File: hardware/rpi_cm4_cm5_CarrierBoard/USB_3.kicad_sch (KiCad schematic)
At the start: 74 parts, among them J2 0484050003, J3 0484050003, U6 SST25VF512A, U7 UPD720202K8-711-BAA-A, U8 AP2192AFGEG-7, Y1 24MHz

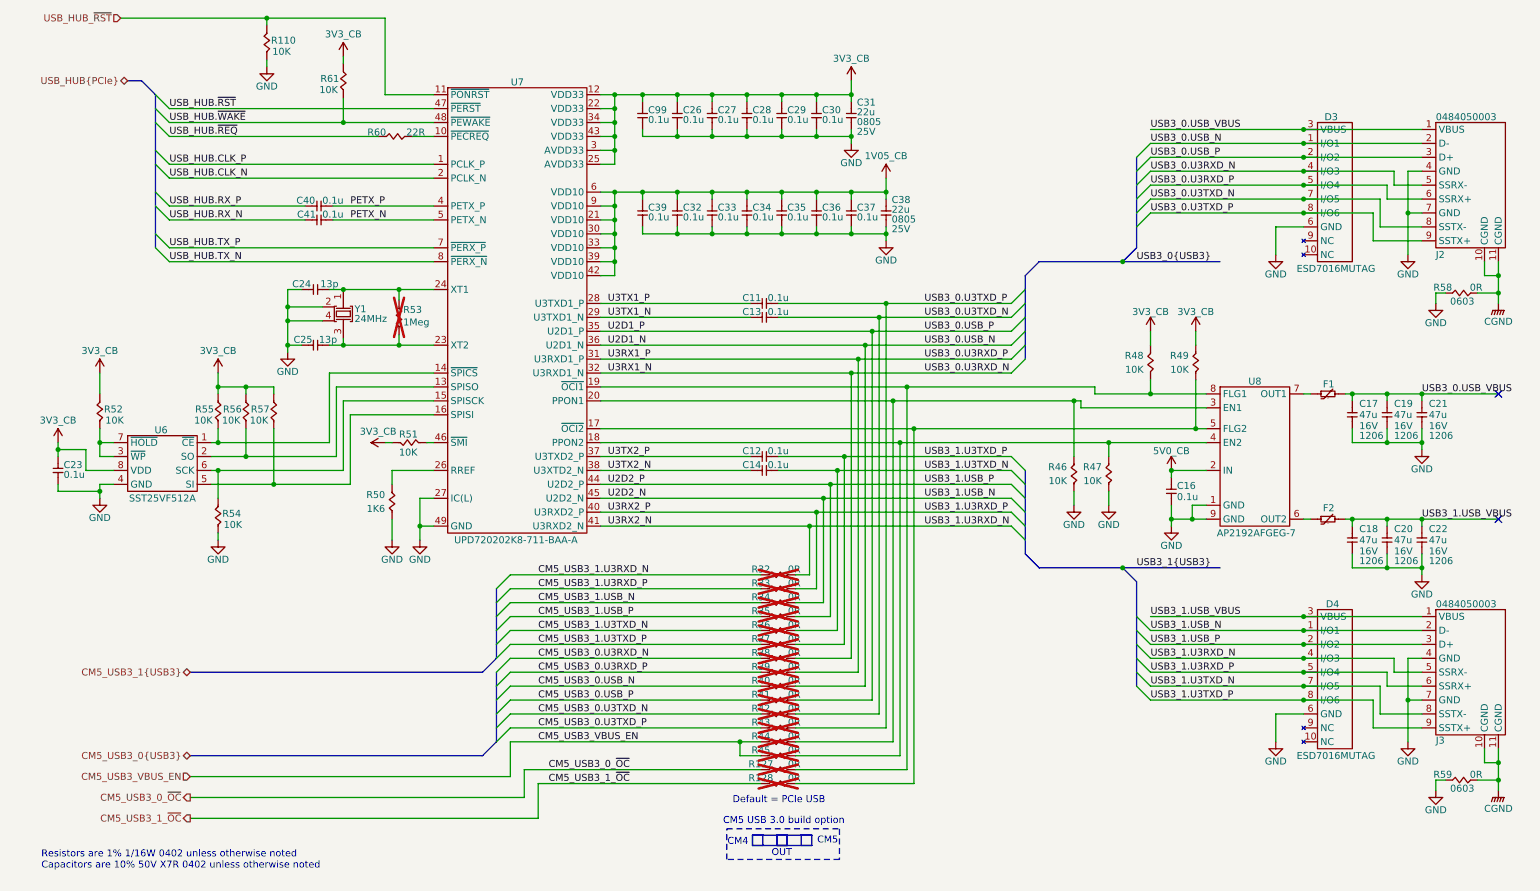
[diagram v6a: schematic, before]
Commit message: Significant update in PCB layout; Completed preliminary high speed rules definition and fanout of differential pairs + GND vias. Started routing high speed signals Slight changes to Pinout based on component placement
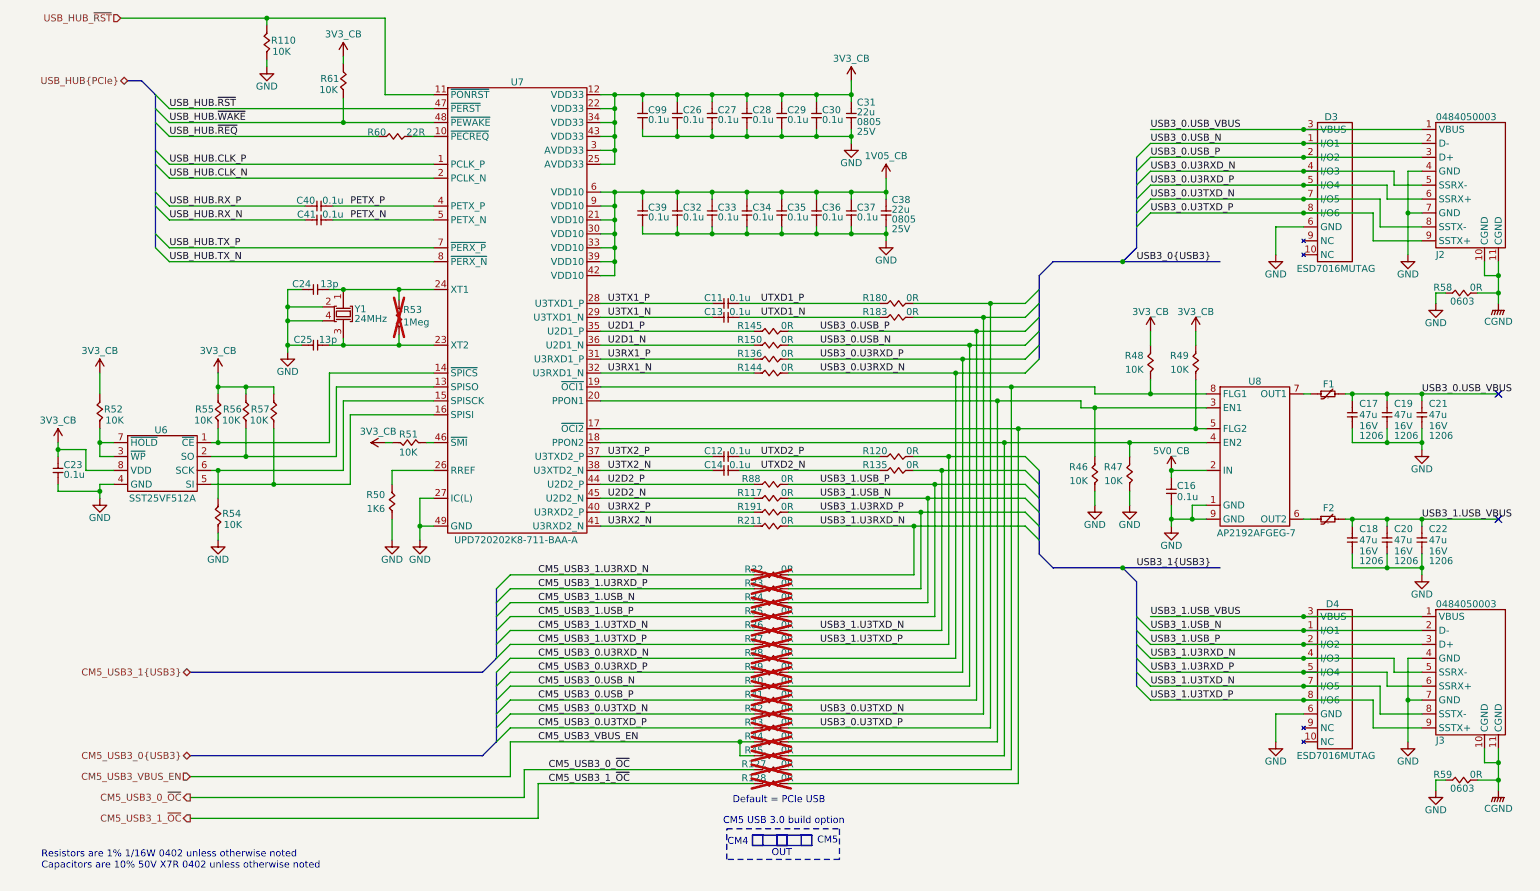
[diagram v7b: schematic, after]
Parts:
- added R117, R120, R135, R136, R144, R145, R150, R180, R183, R211, R32, R88: 0R, footprint:RES_0402, symbol KicadCompDb:Resistors/RES_SMT_00001
- R191: renamed from R32; now fitted
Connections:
- net CM5_USB3_1.U3RXD_N: now also R32.1; no longer R191.1
- net U2D1_N: now also R150.1; no longer D3.1 (I/O1), J2.2 (D-), R40.2
- net U2D1_P: now also R145.1; no longer D3.2 (I/O2), J2.3 (D+), R41.2
- net U2D2_N: now also R117.1; no longer D4.1 (I/O1), J3.2 (D-), R34.2
- net U2D2_P: now also R88.1; no longer D4.2 (I/O2), J3.3 (D+), R35.2
- net U3RX1_N: now also R144.1; no longer D3.4 (I/O3), J2.5 (SSRX-), R38.2
- net U3RX1_P: now also R136.1; no longer D3.5 (I/O4), J2.6 (SSRX+), R39.2
- net U3RX2_N: now also R211.1; no longer D4.4 (I/O3), J3.5 (SSRX-), R191.2
- net U3RX2_P: now also R191.1; no longer D4.5 (I/O4), J3.6 (SSRX+), R33.2
- net USB3_0.U3TXD_N: now also R183.2; no longer C13.2
- net USB3_0.U3TXD_P: now also R180.2; no longer C11.2
- net USB3_1.U3TXD_N: now also R135.2; no longer C14.2
- net USB3_1.U3TXD_P: now also R120.2; no longer C12.2
- new net USB3_0.U3RXD_N: D3.4 (I/O3), J2.5 (SSRX-), R144.2, R38.2
- new net USB3_0.U3RXD_P: D3.5 (I/O4), J2.6 (SSRX+), R136.2, R39.2
- new net USB3_0.USB_N: D3.1 (I/O1), J2.2 (D-), R150.2, R40.2
- new net USB3_0.USB_P: D3.2 (I/O2), J2.3 (D+), R145.2, R41.2
- new net USB3_1.U3RXD_N: D4.4 (I/O3), J3.5 (SSRX-), R211.2, R32.2
- new net USB3_1.U3RXD_P: D4.5 (I/O4), J3.6 (SSRX+), R191.2, R33.2
- new net USB3_1.USB_N: D4.1 (I/O1), J3.2 (D-), R117.2, R34.2
- new net USB3_1.USB_P: D4.2 (I/O2), J3.3 (D+), R35.2, R88.2
- new net UTXD1_N: C13.2, R183.1
- new net UTXD1_P: C11.2, R180.1
- new net UTXD2_N: C14.2, R135.1
- new net UTXD2_P: C12.2, R120.1
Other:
- moved on the sheet: C11, C12, C13, C14, R127, R128, R33, R34, R35, R36, R37, R38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
